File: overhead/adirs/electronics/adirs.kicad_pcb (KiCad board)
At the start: 2 copper layers, 145 x 133 mm, 69 parts, among them J1 Conn_02x01, J2 Conn_02x13_Counter_Clockwise, J3 Conn_02x01, J4 Conn_02x02_Counter_Clockwise, J5 Conn_02x02_Counter_Clockwise, J6 Conn_02x02_Counter_Clockwise

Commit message: Added Gerber for testing purposes. And other optimisations
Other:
- board text added: "Flight Simulation Only"
- board text added: "https://www.gitgub.com/OpenA3XX - ADIRS Panel V1.0"
- board text added: "© 2025 OpenA3XX • CC BY-SA 4.0"
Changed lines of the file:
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@@
 			(outputformat 1)
 			(mirror no)
-			(drillshape 1)
+			(drillshape 0)
 			(scaleselection 1)
-			(outputdirectory "")
+			(outputdirectory "gerber/")
 		)
 	)
@@
 		(layer "F.SilkS")
 	)
-	(gr_curve
-		(pts
-			(xy 161.504926 101.122428) (xy 161.504926 103.62741) (xy 159.474245 105.658087) (xy 156.969267 105.658087)
-		)
-		(stroke
-			(width 0.28)
-			(type solid)
-			(color 0 0 255 1)
-		)
-		(layer "F.SilkS")
-	)
 	(gr_line
 		(start 250.010198 51.01319)
@@
 		(layer "F.SilkS")
 	)
-	(gr_curve
-		(pts
-			(xy 206.869306 101.122428) (xy 206.869306 103.62741) (xy 204.838621 105.658087) (xy 202.333646 105.658087)
-		)
-		(stroke
-			(width 0.28)
-			(type solid)
-			(color 0 0 255 1)
-		)
-		(layer "F.SilkS")
-	)
 	(gr_line
 		(start 200.485586 26.060305)
@@
 		(layer "F.SilkS")
 	)
-	(gr_curve
-		(pts
-			(xy 252.119299 101.122428) (xy 252.119299 103.62741) (xy 250.088628 105.658087) (xy 247.583639 105.658087)
-		)
-		(stroke
-			(width 0.28)
-			(type solid)
-			(color 0 0 255 1)
-		)
-		(layer "F.SilkS")
-	)
 	(gr_line
 		(start 201.784551 121.411856)
@@
 	(gr_curve
 		(pts
-			(xy 247.583639 96.586783) (xy 250.088628 96.586783) (xy 252.119299 98.617461) (xy 252.119299 101.122428)
-		)
-		(stroke
-			(width 0.28)
-			(type solid)
-			(color 0 0 255 1)
-		)
-		(layer "F.SilkS")
-	)
-	(gr_curve
-		(pts
 			(xy 145.488428 89.668929) (xy 145.62256 89.680258) (xy 145.689626 89.753142) (xy 145.689626 89.88758)
 		)
@@
 		(layer "F.SilkS")
 	)
-	(gr_curve
-		(pts
-			(xy 202.333646 105.658087) (xy 199.82868 105.658087) (xy 197.797994 103.62741) (xy 197.797994 101.122428)
-		)
-		(stroke
-			(width 0.28)
-			(type solid)
-			(color 0 0 255 1)
-		)
-		(layer "F.SilkS")
-	)
 	(gr_line
 		(start 156.895116 122.313376)
@@
 		(layer "F.SilkS")
 	)
-	(gr_curve
-		(pts
-			(xy 202.333646 96.586783) (xy 204.838621 96.586783) (xy 206.869306 98.617461) (xy 206.869306 101.122428)
-		)
-		(stroke
-			(width 0.28)
-			(type solid)
-			(color 0 0 255 1)
-		)
-		(layer "F.SilkS")
-	)
 	(gr_line
 		(start 157.038267 121.529807)
@@
 		(layer "F.SilkS")
 	)
-	(gr_curve
-		(pts
-			(xy 156.969267 105.658087) (xy 154.4643 105.658087) (xy 152.433618 103.62741) (xy 152.433618 101.122428)
-		)
-		(stroke
-			(width 0.28)
-			(type solid)
-			(color 0 0 255 1)
-		)
-		(layer "F.SilkS")
-	)
 	(gr_line
 		(start 200.362966 28.875872)
@@
 	(gr_curve
 		(pts
-			(xy 152.433618 101.122428) (xy 152.433618 98.617461) (xy 154.4643 96.586783) (xy 156.969267 96.586783)
-		)
-		(stroke
-			(width 0.28)
-			(type solid)
-			(color 0 0 255 1)
-		)
-		(layer "F.SilkS")
-	)
-	(gr_curve
-		(pts
 			(xy 208.652349 25.673945) (xy 208.445669 25.677031) (xy 208.28758 25.76649) (xy 208.178075 25.942317)
 		)
@@
 	(gr_curve
 		(pts
-			(xy 156.969267 96.586783) (xy 159.474245 96.586783) (xy 161.504926 98.617461) (xy 161.504926 101.122428)
-		)
-		(stroke
-			(width 0.28)
-			(type solid)
-			(color 0 0 255 1)
-		)
-		(layer "F.SilkS")
-	)
-	(gr_curve
-		(pts
 			(xy 207.343939 120.978797) (xy 207.343939 121.106986) (xy 207.300909 121.22251) (xy 207.214842 121.32537)
 		)
@@
 	(gr_curve
 		(pts
-			(xy 247.583639 105.658087) (xy 245.07868 105.658087) (xy 243.047994 103.62741) (xy 243.047994 101.122428)
-		)
-		(stroke
-			(width 0.28)
-			(type solid)
-			(color 0 0 255 1)
-		)
-		(layer "F.SilkS")
-	)
-	(gr_curve
-		(pts
 			(xy 200.87795 83.206549) (xy 200.87795 83.310042) (xy 200.831091 83.375838) (xy 200.737371 83.403929)
 		)
@@
 		(layer "F.SilkS")
 	)
-	(gr_curve
-		(pts
-			(xy 243.047994 101.122428) (xy 243.047994 98.617461) (xy 245.07868 96.586783) (xy 247.583639 96.586783)
-		)
-		(stroke
-			(width 0.28)
-			(type solid)
-			(color 0 0 255 1)
-		)
-		(layer "F.SilkS")
-	)
 	(gr_line
 		(start 209.655264 27.322337)
@@
 		(layer "F.SilkS")
 	)
-	(gr_curve
-		(pts
-			(xy 197.797994 101.122428) (xy 197.797994 98.617461) (xy 199.82868 96.586783) (xy 202.333646 96.586783)
-		)
-		(stroke
-			(width 0.28)
-			(type solid)
-			(color 0 0 255 1)
-		)
-		(layer "F.SilkS")
-	)
 	(gr_line
 		(start 156.98921 122.033759)
@@
 		(layer "Edge.Cuts")
 	)
+	(gr_text "https://www.gitgub.com/OpenA3XX - ADIRS Panel V1.0"
+		(at 134.7 122 90)
+		(layer "F.SilkS")
+		(effects
+			(font
+				(size 1.5 1.5)
+				(thickness 0.3)
+				(bold yes)
+			)
+			(justify left bottom)
+		)
+	)
 	(gr_text "ON_BAT INDICATOR"
 		(at 201.5 36.8 0)
@@
 		)
 	)
+	(gr_text "Flight Simulation Only"
+		(at 270.7 108.3 90)
+		(layer "F.SilkS")
+		(effects
+			(font
+				(size 1.5 1.5)
+				(thickness 0.3)
+				(bold yes)
+			)
+			(justify left bottom)
+		)
+	)
+	(gr_text "© 2025 OpenA3XX • CC BY-SA 4.0"
+		(at 270.1 57.8 90)
+		(layer "F.SilkS")
+		(effects
+			(font
+				(size 1.27 1.27)
+			)
+		)
+	)
+	(gr_text "Flight Simulation Only"
+		(at 268.8 108.3 -90)
+		(layer "B.SilkS")
+		(effects
+			(font
+				(size 1.5 1.5)
+				(thickness 0.3)
+				(bold yes)
+			)
+			(justify left bottom mirror)
+		)
+	)
+	(gr_text "https://www.gitgub.com/OpenA3XX - ADIRS Panel V1.0"
+		(at 132.8 122 -90)
+		(layer "B.SilkS")
+		(effects
+			(font
+				(size 1.5 1.5)
+				(thickness 0.3)
+				(bold yes)
+			)
+			(justify left bottom mirror)
+		)
+	)
 	(gr_text "GND"
 		(at 157.9 25.4 -0)
@@
 		)
 	)
+	(gr_text "© 2025 OpenA3XX • CC BY-SA 4.0"
+		(at 270 57.8 -90)
+		(layer "B.SilkS")
+		(effects
+			(font
+				(size 1.27 1.27)
+			)
+			(justify mirror)
+		)
+	)
 	(gr_text "+12V \nVariable Backlight"
 		(at 143.6 25.5 -0)
@@
 	)
 	(segment
+		(start 149.16 25.3)
+		(end 149.16 47.305)
+		(width 0.2)
+		(layer "B.Cu")
+		(net 1)
+	)
+	(segment
 		(start 175.05 135.25)
 		(end 187.6 147.8)
@@
 		(width 0.2)
 		(layer "B.Cu")
-		(net 1)
-	)
-	(segment
-		(start 149.16 25.3)
-		(end 149.16 47.305)
-		(width 0.2)
-		(layer "B.Cu")

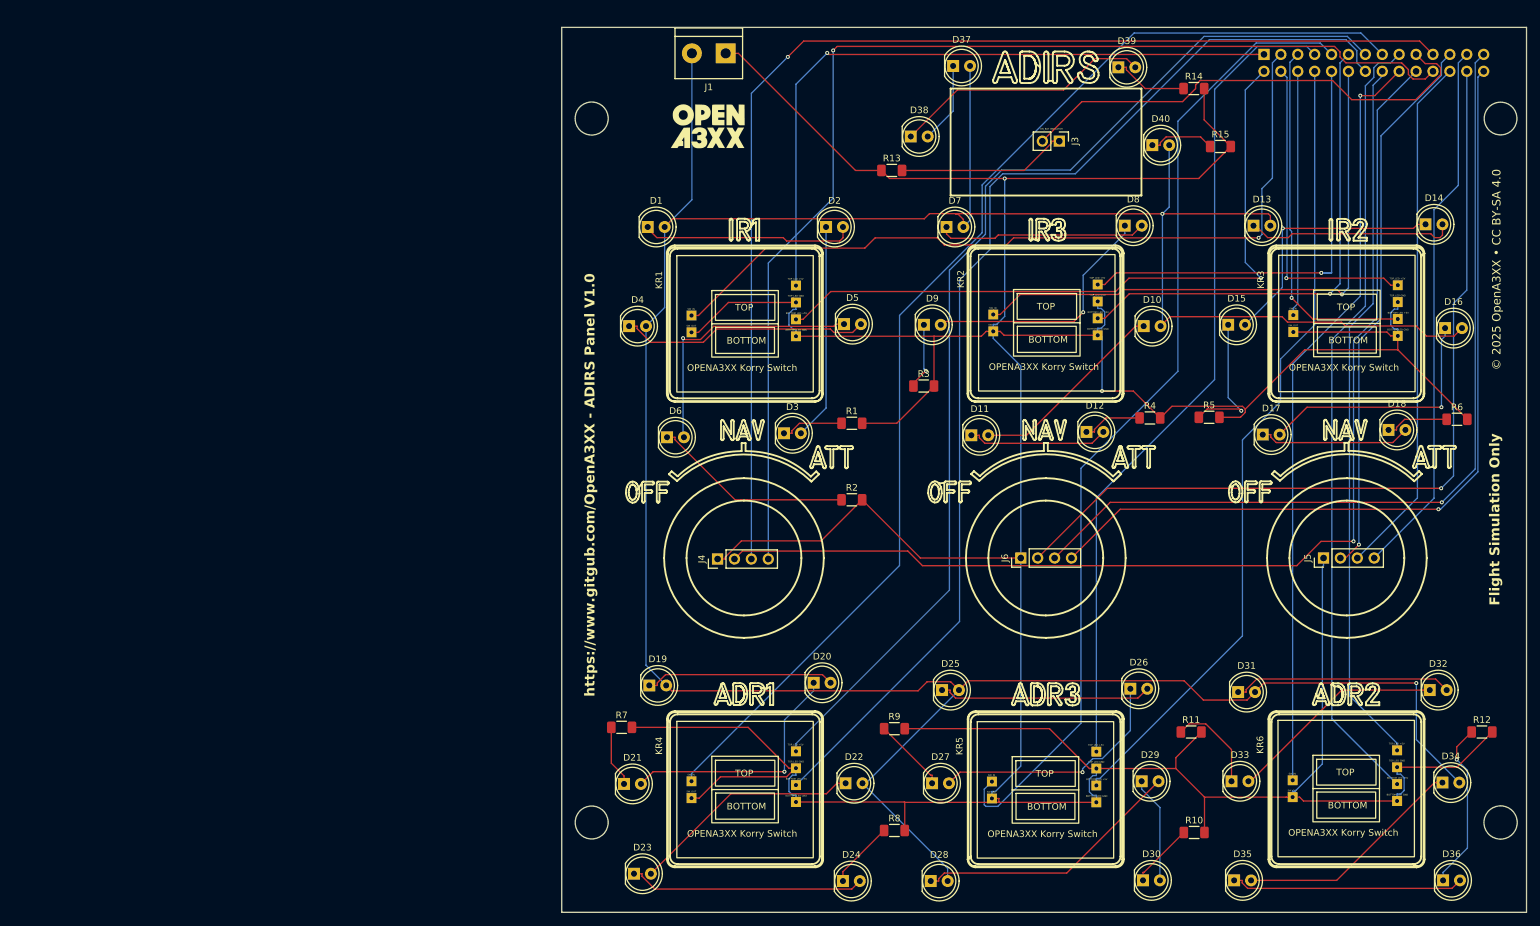
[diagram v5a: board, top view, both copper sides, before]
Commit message: Finalised ROuting for FLT-CTL CPT Side, and cleaned up ADIRS Panel PCB
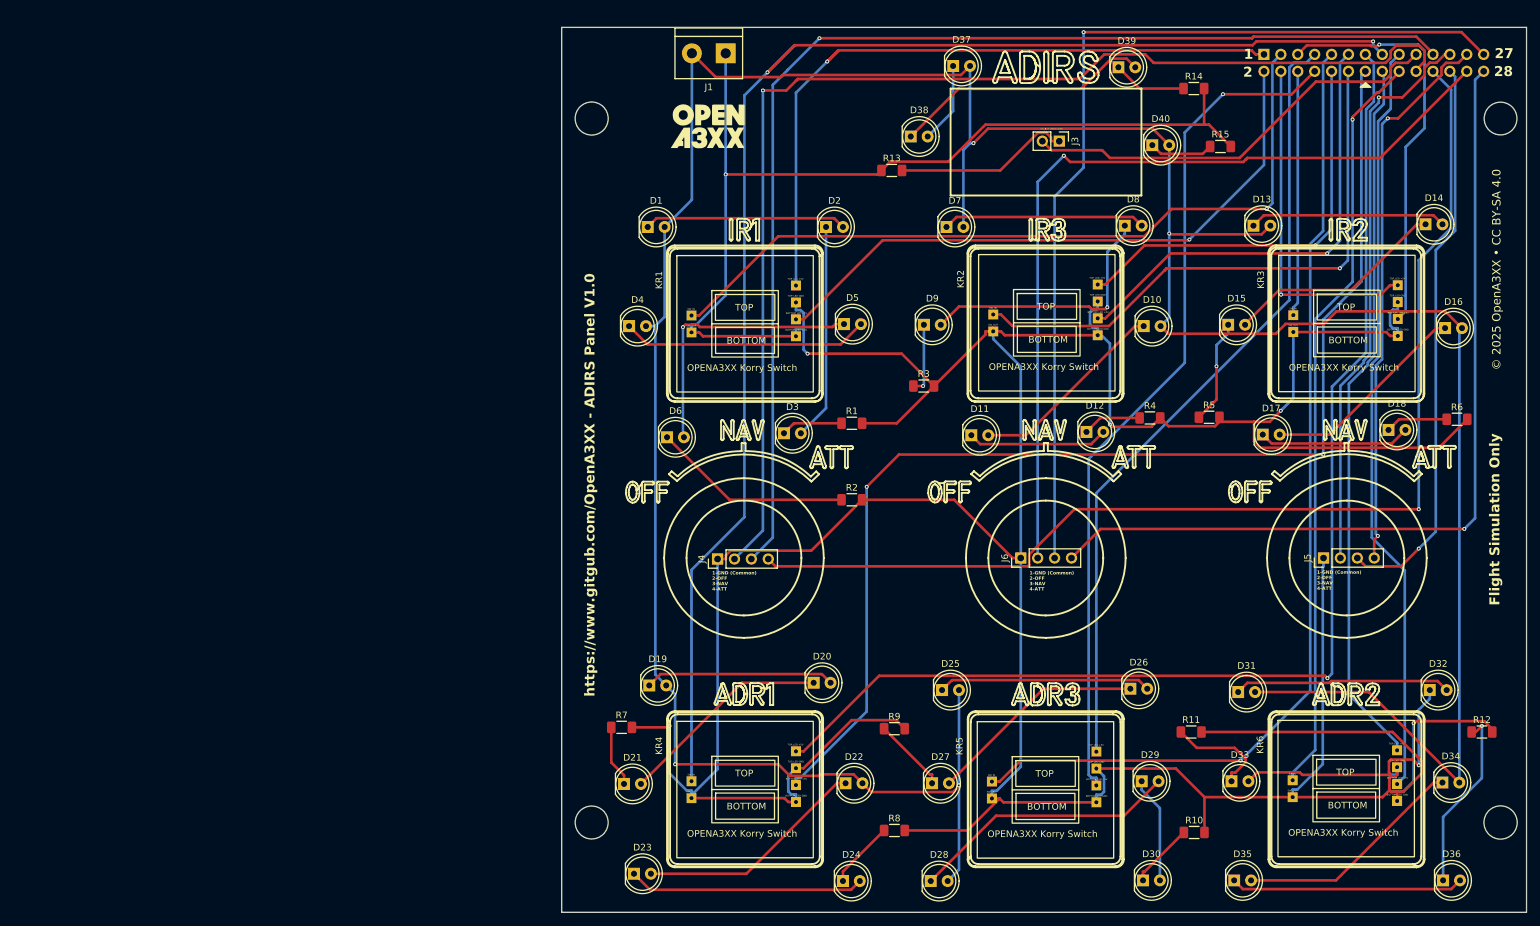
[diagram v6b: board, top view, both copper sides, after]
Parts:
- renumbered G*** to Bottom
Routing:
- net GND: track 708.8 -> 775.6 mm, vias 2 -> 6
- net Net-(J2-Pin_15): track 178.6 -> 229.8 mm, vias 0 -> 2
- net Net-(J2-Pin_13): track 164.3 -> 181.9 mm, vias 0 -> 1
- net +12V: track 470.9 -> 483.2 mm, vias 2 -> 4
- net Net-(J2-Pin_2): track 105.7 -> 94.0 mm
- net Net-(J2-Pin_27): track 131.6 -> 142.3 mm
- net Net-(J2-Pin_14): track 170.6 -> 180.5 mm, vias 0 -> 2
- net Net-(J2-Pin_20): track 170.5 -> 180.3 mm
- net Net-(J2-Pin_1): track 102.7 -> 111.7 mm
- net Net-(D32-K): track 32.9 -> 41.0 mm, vias 0 -> 1
- net Net-(J2-Pin_19): track 72.3 -> 64.3 mm
- net Net-(J2-Pin_5): track 54.5 -> 62.1 mm
- net Net-(J2-Pin_8): track 121.2 -> 128.4 mm, vias 0 -> 1
- net Net-(D16-K): track 38.1 -> 31.5 mm, vias 1 -> 0
- net Net-(J2-Pin_24): track 78.9 -> 85.2 mm, vias 0 -> 1
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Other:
- board text added: "1"
- board text added: "1-GND (Common) 2-OFF 3-NAV 4-ATT"
- board text added: "1-IR1-TOP_LED 2-IR1-BOTTOM_LED 3-IR1-KORRY_SW 4-IR2-TOP_LED 5-IR2-BOTTOM_LED 6-IR2-KORRY_SW 7-IR3-TOP_LED 8-IR3-BOTTOM_LED 9-IR3-KORRY_SW 10-ADR1-TOP_LED 11-ADR1-BOTTOM_LED 12-ADR1-KORRY_SW 13-ADR2-TOP_LED 14-ADR2-BOTTOM_LED"
- board text added: "15-ADR2-KORRY_SW 16-ADR3-TOP_LED 17-ADR3-BOTTOM_LED 18-ADR3-KORRY_SW 19-ON_BAT_LED 20-ADR1-RS-OFF 21-ADR1-RS-NAV 22-ADR1-RS-ATT 23-ADR2-RS-OFF 24-ADR2-RS-NAV 25-ADR2-RS-ATT 26-ADR3-RS-OFF 27-ADR3-RS-NAV 28-ADR3-RS-ATT"
- board text added: "2"
- board text added: "27"
- board text added: "28"

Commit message: Updated all LEDs for SMD!
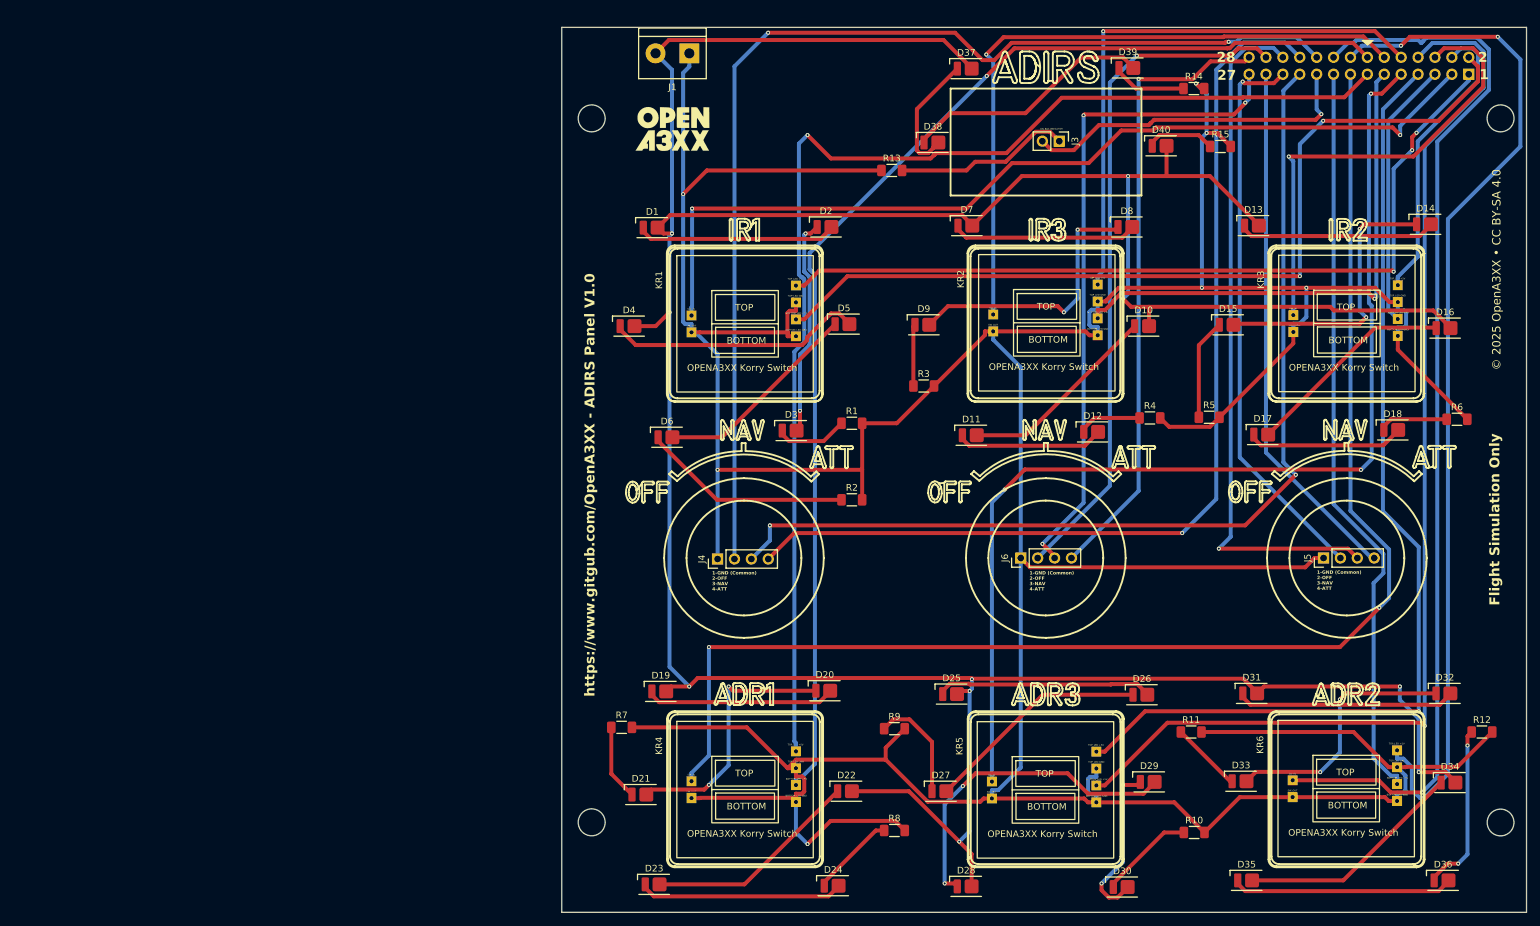
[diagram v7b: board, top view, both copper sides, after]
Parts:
- D1, D10, D11, D12, D13, D14, D15, D16, D17, D18, D19, D2, D20, D21, D22, D23, D24, D25, D26, D27, D28, D29, D3, D30, D31, D32, D33, D34, D35, D36, D37, D38, D39, D4, D40, D5, D6, D7, D8, D9: footprint LED_THT:LED_D5.0mm_Clear -> OpenA3XX:LED_Everlight-SMD3528_3.5x2.8mm_67-21ST
- moved J2 30.9 mm to (265.9, 28.4), turned to 90 degrees
- moved J1 5.46 mm to (148.8, 25.3)
- moved D28 5.39 mm to (190.4, 150.5)
- moved Bottom 5.32 mm to (146.3, 36.6)
- moved G*** 5.32 mm to (146.3, 36.6)
- moved D38 3.45 mm to (185.4, 38.7)
- moved D23 3.43 mm to (143.5, 150.2)
- moved D30 3.28 mm to (213.8, 150.6)
- moved D7 3.07 mm to (190.5, 51.2)
- moved D21 3.00 mm to (141.5, 136.7)
- moved D32 2.33 mm to (262.3, 121.5)
- moved D20 2.06 mm to (169.1, 121.1)
- moved D31 2.05 mm to (233.3, 121.5)
- moved D37 2.02 mm to (190.4, 27.6)
- moved D26 1.96 mm to (216.8, 121.7)
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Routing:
- net GND: track 775.6 -> 721.1 mm, vias 6 -> 7
- net Net-(J2-Pin_18): track 113.3 -> 162.6 mm
- net Net-(J2-Pin_16): track 107.3 -> 155.0 mm, vias 0 -> 2
- net Net-(J2-Pin_27): track 142.3 -> 99.5 mm, vias 1 -> 3
- net Net-(J2-Pin_8): track 128.4 -> 169.7 mm
- net Net-(J2-Pin_2): track 94.0 -> 133.1 mm, vias 1 -> 2
- net Net-(J2-Pin_28): track 130.8 -> 94.2 mm
- net +12V: track 483.2 -> 518.6 mm, vias 4 -> 10
- net Net-(J2-Pin_6): track 36.9 -> 70.4 mm, vias 0 -> 1
- net Net-(J2-Pin_7): track 119.5 -> 151.1 mm, vias 0 -> 1
- net Net-(J2-Pin_26): track 129.0 -> 102.1 mm
- net Net-(J2-Pin_21): track 176.4 -> 150.4 mm, vias 1 -> 2
- net Net-(J2-Pin_3): track 117.2 -> 140.4 mm, vias 1 -> 2
- net Net-(J2-Pin_10): track 62.3 -> 84.8 mm
- net Net-(J2-Pin_15): track 229.8 -> 207.6 mm
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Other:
- outline, holes or cut-outs redrawn

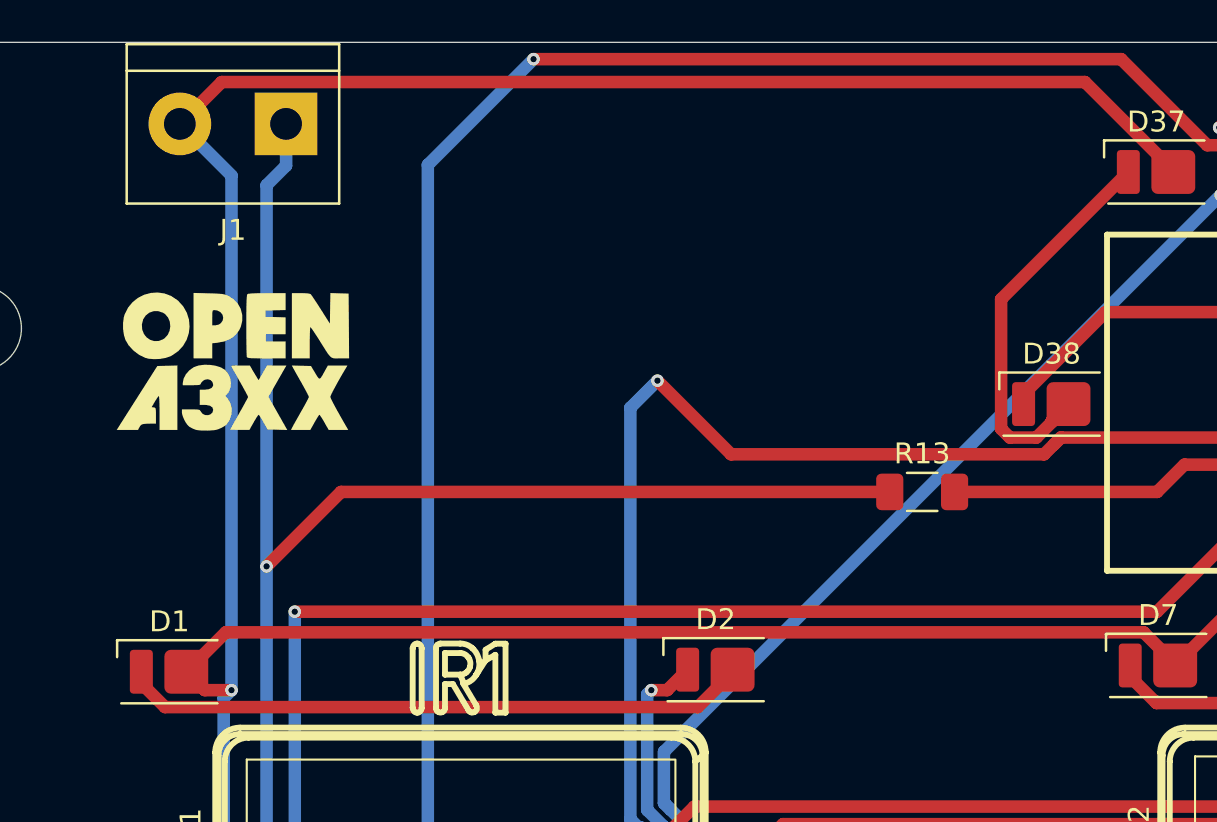
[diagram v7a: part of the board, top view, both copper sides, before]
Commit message: Added terminal connector to 3D models
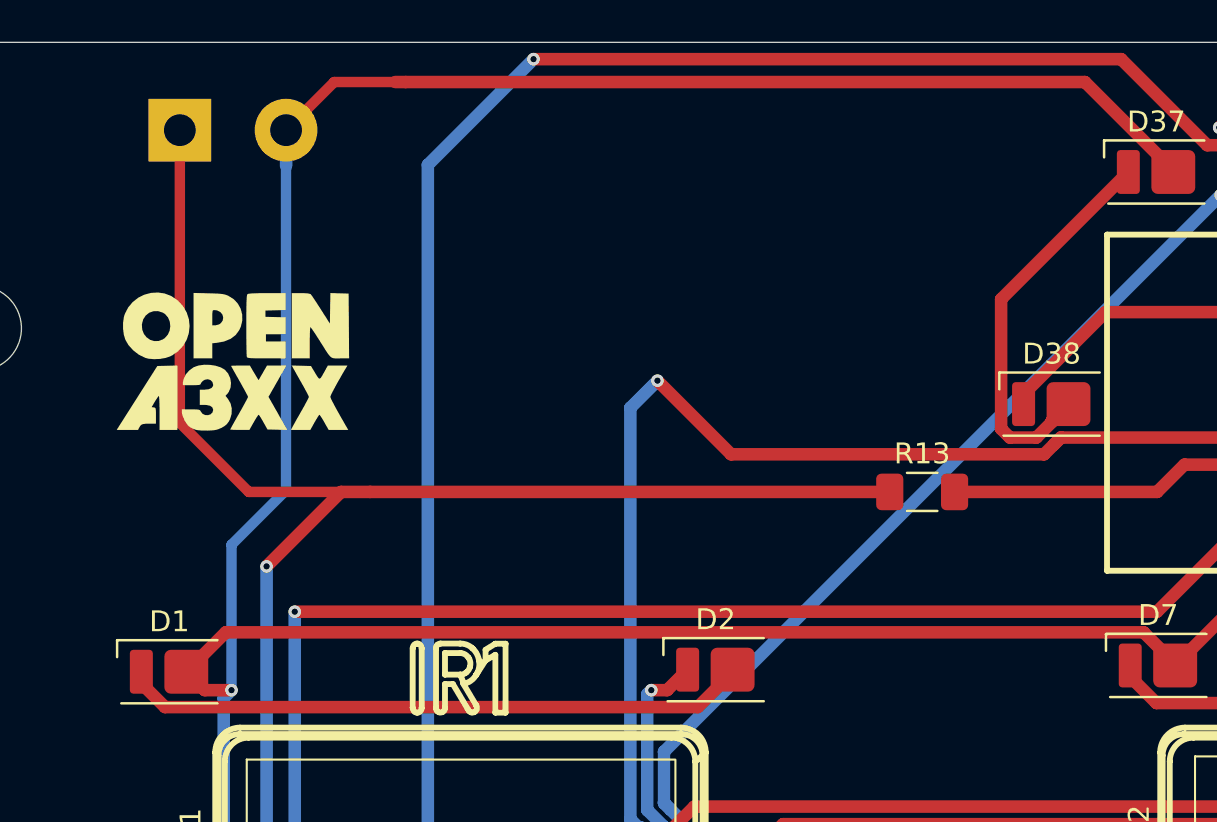
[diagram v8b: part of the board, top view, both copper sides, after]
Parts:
- J1: moved to B.Cu
- moved J1 5.09 mm to (143.7, 25.6), turned to 0 degrees
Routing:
- net GND: track 721.1 -> 724.2 mm
